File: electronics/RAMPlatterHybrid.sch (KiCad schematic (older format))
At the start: 53 parts, among them J1 Raspberry_Pi_2_3, U1 LM358, U2 74LVC74APW, U3 AV2-8.4-10, U4 AV2-8.4-10, U5 HC4046A, U6 CD74HC4059, U7 AP1117-33, U8 WM8750, U9 NE567

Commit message: v1.0
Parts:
- added J2: Raspberry_Pi_2_3, Connector_PinHeader_2.54mm:PinHeader_2x20_P2.54mm_Vertical, symbol Connector:Raspberry_Pi_2_3
- added JP3: SolderJumper_2_Bridged, Jumper:SolderJumper-2_P1.3mm_Bridged_Pad1.0x1.5mm, symbol Jumper:SolderJumper_2_Bridged
- C10, C16, C8: footprint (none) -> Capacitor_SMD:CP_Elec_4x5.3
- C11, C12, C13, C14: value 1u -> 1u NP; footprint (none) -> Capacitor_SMD:CP_Elec_5x5.3
- C24: footprint Capacitor_SMD:C_0603_1608Metric -> (none)
- C26: renamed from C22; footprint Capacitor_SMD:C_0603_1608Metric -> (none)
- J1: footprint Connector_PinHeader_2.54mm:PinHeader_2x20_P2.54mm_Vertical -> 40pin.SMD.rev:02x20.SMD.pinLocsRev
- R10, R7, R8, R9: value 47R -> 75R
- R13, R14, R15: footprint Resistor_SMD:R_0603_1608Metric -> (none)
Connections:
- net +3V3: now also J2.17 (3V3); no longer J1.1 (3V3)
- net +5V: now also J2.2 (5V), J2.4 (5V)
- net GND: now also J2.14 (GND), J2.20 (GND), J2.25 (GND), J2.30 (GND), J2.34 (GND), J2.39 (GND), J2.6 (GND), J2.9 (GND), JP3.2 (B)
- net GNDA: now also JP3.1 (A)
- net HIGH: now also U6.14 (KA)
- net LOW: no longer U6.14 (KA)
- net SCL: now also J2.5 (SCL/GPIO3)
- net SDA: now also J2.3 (SDA/GPIO2)
- net at J1.10 (GPIO15/RXD): now also J2.10 (GPIO15/RXD)
- net at J1.11 (GPIO17): now also J2.11 (GPIO17)
- net at J1.13 (GPIO27): now also J2.13 (GPIO27)
- net at J1.15 (GPIO22): now also J2.15 (GPIO22)
- net at J1.16 (GPIO23): now also J2.16 (GPIO23)
- net at J1.18 (GPIO24): now also J2.18 (GPIO24)
- net at J1.19 (MOSI0/GPIO10): now also J2.19 (MOSI0/GPIO10)
- net at J1.21 (MISO0/GPIO9): now also J2.21 (MISO0/GPIO9)
- net at J1.22 (GPIO25): now also J2.22 (GPIO25)
- net at J1.23 (SCLK0/GPIO11): now also J2.23 (SCLK0/GPIO11)
- net at J1.24 (~CE0~/GPIO8): now also J2.24 (~CE0~/GPIO8)
- net at J1.26 (~CE1~/GPIO7): now also J2.26 (~CE1~/GPIO7)
- net at J1.27 (ID_SD/GPIO0): now also J2.27 (ID_SD/GPIO0)
- net at J1.28 (ID_SC/GPIO1): now also J2.28 (ID_SC/GPIO1)
- net at J1.29 (GCLK1/GPIO5): now also J2.29 (GCLK1/GPIO5)
- net at J1.31 (GCLK2/GPIO6): now also J2.31 (GCLK2/GPIO6)
- net at J1.32 (PWM0/GPIO12): now also J2.32 (PWM0/GPIO12)
- net at J1.33 (PWM1/GPIO13): now also J2.33 (PWM1/GPIO13)
- net at J1.36 (GPIO16): now also J2.36 (GPIO16)
- net at J1.7 (GCLK0/GPIO4): now also J2.7 (GCLK0/GPIO4)
- net at J1.8 (GPIO14/TXD): now also J2.8 (GPIO14/TXD)
- net AVDD: now reaches C4.1, C5.1, C6.1, C8.1, U7.2 (VO), U8.17 (HPVDD), U8.18 (AVDD)
- new net: J1.1 (3V3), J2.1 (3V3)
- no-connect marks 15 -> 20

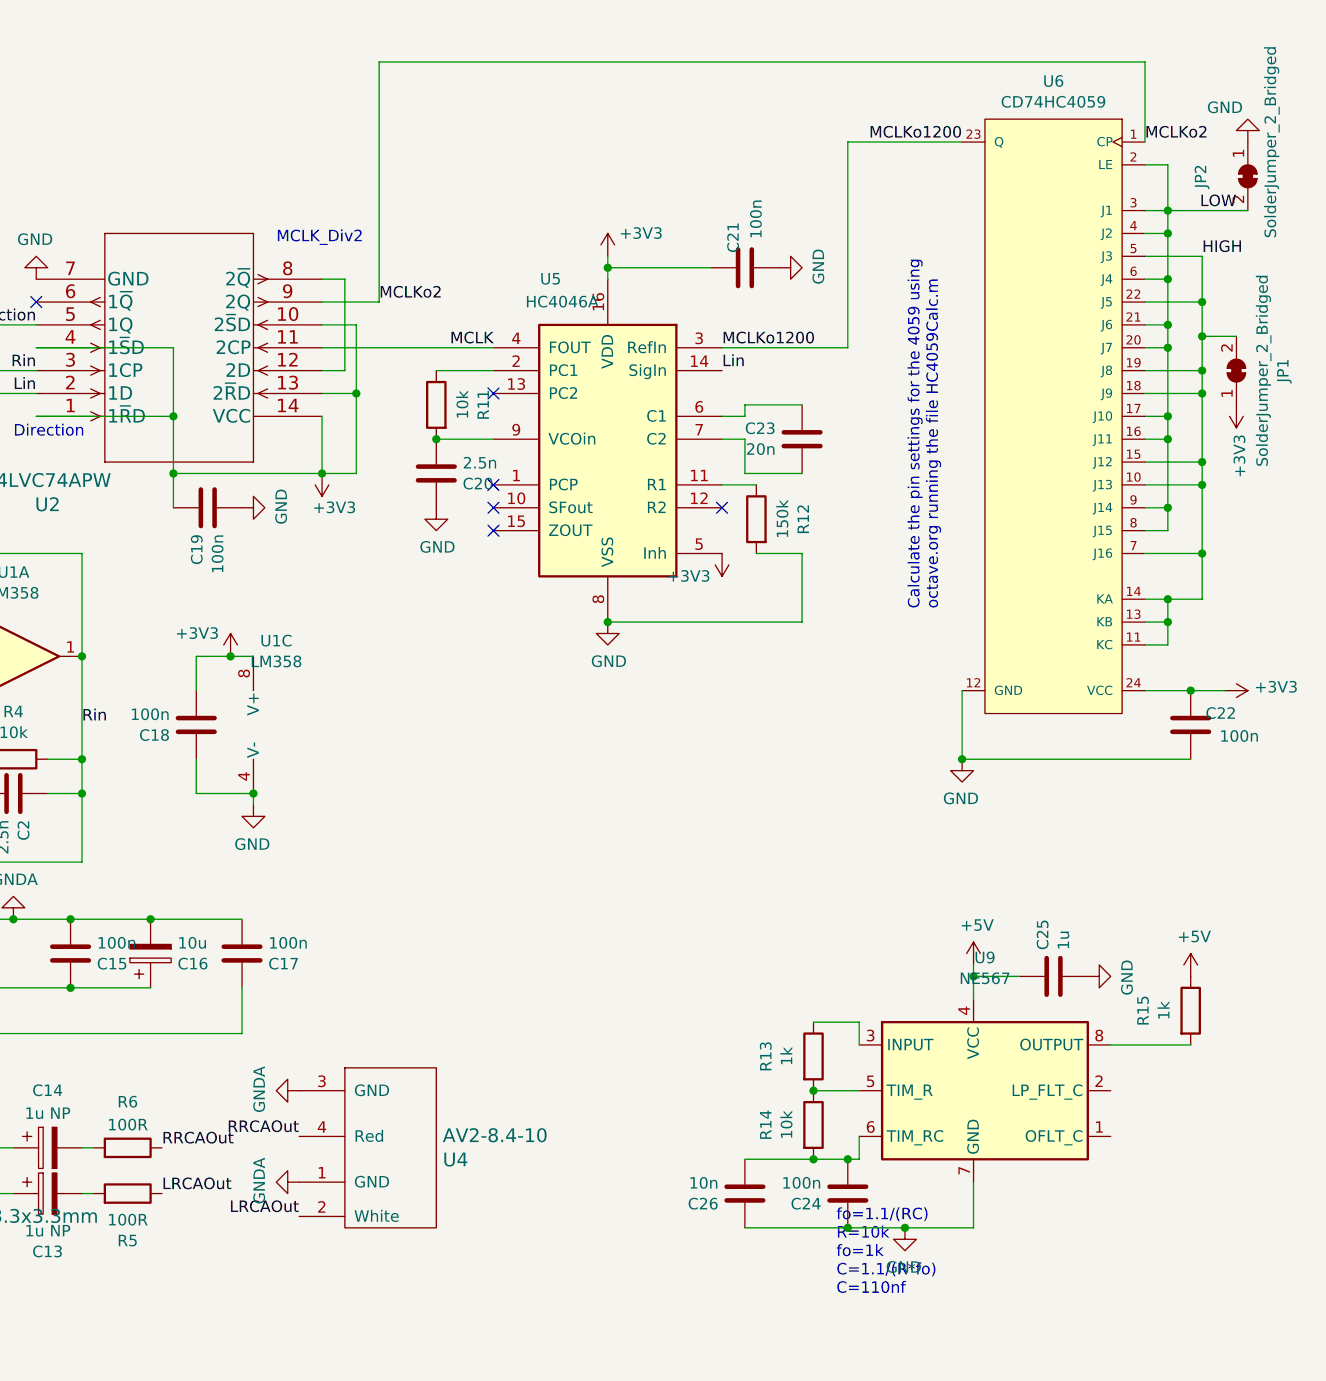
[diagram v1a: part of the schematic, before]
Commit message: v1.1 Many hardware bug fixes, 4059 now dividing correctly. 4046 voc on better target, still debugging 4046 PLL.
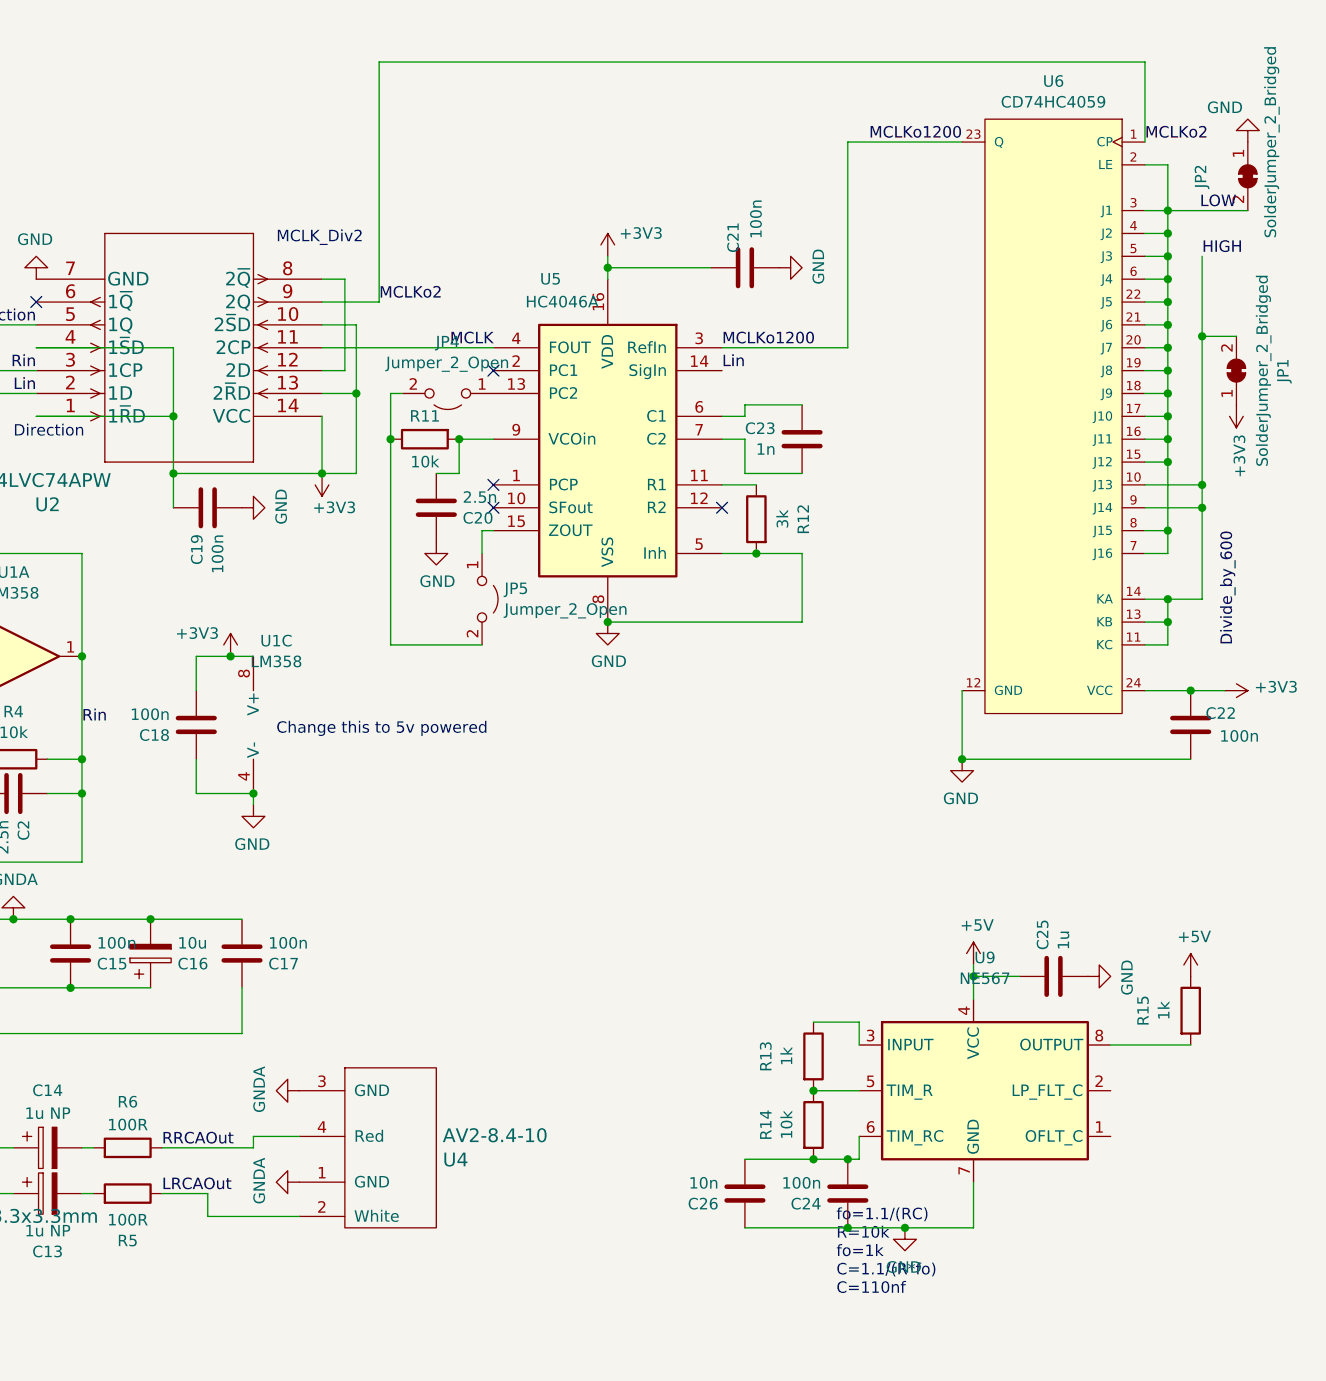
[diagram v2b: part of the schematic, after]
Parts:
- added JP4, JP5: Jumper_2_Open, Jumper:SolderJumper-2_P1.3mm_Open_Pad1.0x1.5mm, symbol Jumper:Jumper_2_Open
- C23: value 20n -> 1n
- R12: value 150k -> 3k
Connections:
- net +3V3: no longer U5.5 (Inh)
- net GND: now also U5.5 (Inh)
- net HIGH: now also U6.9 (J14); no longer U6.15 (J12), U6.18 (J9), U6.19 (J8), U6.22 (J5), U6.5 (J3), U6.7 (J16)
- net LOW: now also U6.15 (J12), U6.18 (J9), U6.19 (J8), U6.22 (J5), U6.5 (J3), U6.7 (J16); no longer U6.9 (J14)
- net at U5.13 (PC2): now also JP4.1 (A)
- net at U5.15 (ZOUT): now also JP5.1 (A)
- net at U5.2 (PC1): no longer R11.1
- new net: JP4.2 (B), JP5.2 (B), R11.1
- no-connect marks 20 -> 19
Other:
- note added: "Change this to 5v powered"
- note removed: "Calculate the pin settings for the 4059 using\noctave.org running the file HC4059Calc.m"
- moved on the sheet: C20, R11
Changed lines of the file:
@@
 Text Label 3450 5050 2    50   ~ 0
 Lin
-Text Label 6850 5800 2    50   ~ 0
-LRCAOut
-Text Label 6850 5450 2    50   ~ 0
-RRCAOut
 $Comp
 L power:GNDA #PWR0117
@@
 	1    0    0    -1
 $EndComp
-$Comp
-L power:+3V3 #PWR0114
-U 1 1 619323EE
-P 8700 2900
-F 0 "#PWR0114" H 8700 2750 50  0001 C CNN
-F 1 "+3V3" H 8750 3000 50  0000 L CNN
-F 2 "" H 8700 2900 50  0001 C CNN
-F 3 "" H 8700 2900 50  0001 C CNN
-	1    8700 2900
-	-1   0    0    1
-$EndComp
 Wire Wire Line
 	9050 2900 9050 3200
@@
 	8850 2600 8700 2600
 NoConn ~ 7700 2600
-NoConn ~ 7700 2200
-Wire Wire Line
-	7450 2400 7700 2400
-Wire Wire Line
-	7700 2100 7450 2100
 Text Label 8700 2000 0    50   ~ 0
 MCLKo1200
@@
 P 8850 2750
 F 0 "R12" V 8643 2750 50  0000 C CNN
-F 1 "150k" V 8734 2750 50  0000 C CNN
+F 1 "3k" V 8734 2750 50  0000 C CNN
 F 2 "Resistor_SMD:R_0603_1608Metric" V 8780 2750 50  0001 C CNN
 F 3 "~" H 8850 2750 50  0001 C CNN
@@
 P 9050 2400
 F 0 "C23" H 9165 2446 50  0000 L CNN
-F 1 "20n" H 9165 2355 50  0000 L CNN
+F 1 "1n" H 9165 2355 50  0000 L CNN
 F 2 "Capacitor_SMD:C_0603_1608Metric" H 9088 2250 50  0001 C CNN
 F 3 "~" H 9050 2400 50  0001 C CNN
@@
 L Device:C C20
 U 1 1 61B4B373
-P 7450 2550
-F 0 "C20" H 7565 2596 50  0000 L CNN
-F 1 "2.5n" H 7565 2505 50  0000 L CNN
-F 2 "Capacitor_SMD:C_0603_1608Metric" H 7488 2400 50  0001 C CNN
-F 3 "~" H 7450 2550 50  0001 C CNN
-	1    7450 2550
-	1    0    0    1
-$EndComp
-Connection ~ 7450 2400
+P 7450 2700
+F 0 "C20" H 7565 2746 50  0000 L CNN
+F 1 "2.5n" H 7565 2655 50  0000 L CNN
+F 2 "Capacitor_SMD:C_0603_1608Metric" H 7488 2550 50  0001 C CNN
+F 3 "~" H 7450 2700 50  0001 C CNN
+	1    7450 2700
+	1    0    0    1
+$EndComp
 $Comp
 L Device:R R11
 U 1 1 61B4AD34
-P 7450 2250
-F 0 "R11" V 7243 2250 50  0000 C CNN
-F 1 "10k" V 7334 2250 50  0000 C CNN
-F 2 "Resistor_SMD:R_0603_1608Metric" V 7380 2250 50  0001 C CNN
-F 3 "~" H 7450 2250 50  0001 C CNN
-	1    7450 2250
-	-1   0    0    -1
+P 7400 2400
+F 0 "R11" V 7300 2400 50  0000 C CNN
+F 1 "10k" V 7500 2400 50  0000 C CNN
+F 2 "Resistor_SMD:R_0603_1608Metric" V 7330 2400 50  0001 C CNN
+F 3 "~" H 7400 2400 50  0001 C CNN
+	1    7400 2400
+	0    -1   1    0
 $EndComp
 $Comp
@@
 	-1   0    0    -1
 $EndComp
-NoConn ~ 7700 2800
 NoConn ~ 7700 2700
 $Comp
 L power:GND #PWR0113
 U 1 1 61900830
-P 7450 2700
-F 0 "#PWR0113" H 7450 2450 50  0001 C CNN
-F 1 "GND" H 7455 2527 50  0000 C CNN
-F 2 "" H 7450 2700 50  0001 C CNN
-F 3 "" H 7450 2700 50  0001 C CNN
-	1    7450 2700
+P 7450 2850
+F 0 "#PWR0113" H 7450 2600 50  0001 C CNN
+F 1 "GND" H 7455 2677 50  0000 C CNN
+F 2 "" H 7450 2850 50  0001 C CNN
+F 3 "" H 7450 2850 50  0001 C CNN
+	1    7450 2850
 	1    0    0    -1
 $EndComp
@@
 Wire Wire Line
 	10650 2800 10550 2800
-Wire Wire Line
-	10650 2700 10650 2800
-Connection ~ 10650 2700
-Wire Wire Line
-	10650 2700 10550 2700
 $Comp
 L Jumper:SolderJumper_2_Bridged JP1
@@
 Text Label 10800 1600 0    50   ~ 0
 HIGH
-Text Notes 9650 3150 1    50   ~ 0
-Calculate the pin settings for the 4059 using\noctave.org running the file HC4059Calc.m
 $Comp
 L power:+3V3 #PWR05
@@
 	1    0    0    1
 $EndComp
-Wire Wire Line
-	10800 1600 10550 1600
-Wire Wire Line
-	10800 1800 10800 1950
-Wire Wire Line
-	10800 1800 10800 1600
-Connection ~ 10800 1800
-Wire Wire Line
-	10800 1800 10550 1800
-Wire Wire Line
-	10800 1950 10800 2100
-Connection ~ 10800 2100
-Wire Wire Line
-	10800 2100 10550 2100
-Wire Wire Line
-	10800 2200 10800 2100
-Connection ~ 10800 2200
-Wire Wire Line
-	10800 2200 10550 2200
-Wire Wire Line
-	10800 2500 10800 2200
-Connection ~ 10800 2500
-Wire Wire Line
-	10800 2500 10550 2500
-Wire Wire Line
-	10800 2600 10800 2500
 Connection ~ 10800 2600
 Wire Wire Line
@@
 	1    0    0    1
 $EndComp
-Wire Wire Line
-	10650 2400 10650 2700
 Connection ~ 10650 2400
 Wire Wire Line
@@
 	10650 2300 10550 2300
 Wire Wire Line
-	10650 2000 10650 2300
+	10650 2000 10650 2100
 Connection ~ 10650 2000
 Wire Wire Line
@@
 	10650 1900 10550 1900
 Wire Wire Line
-	10650 1700 10650 1900
+	10650 1700 10650 1800
 Connection ~ 10650 1700
 Wire Wire Line
 	10650 1700 10550 1700
 Wire Wire Line
-	10650 1500 10650 1700
+	10650 1500 10650 1600
 Wire Wire Line
 	10650 1400 10650 1500
@@
 Wire Wire Line
 	10650 3100 10550 3100
-Wire Wire Line
-	10800 2900 10800 2600
-Wire Wire Line
-	10550 2900 10800 2900
 $Comp
 L Device:C C22
@@
 Wire Wire Line
 	10650 3100 10800 3100
-Wire Wire Line
-	10800 3100 10800 2900
 Connection ~ 10650 3100
-Connection ~ 10800 2900
 Wire Wire Line
 	10550 3200 10650 3200
@@
 Wire Wire Line
 	1950 6200 1950 6000
+Text Notes 6750 3700 0    50   ~ 0
+Change this to 5v powered
+Wire Wire Line
+	10800 1600 10800 1950
+Wire Wire Line
+	10800 1950 10800 2600
+Wire Wire Line
+	10650 2400 10650 2500
+Wire Wire Line
+	10550 1600 10650 1600
+Connection ~ 10650 1600
+Wire Wire Line
+	10650 1600 10650 1700
+Wire Wire Line
+	10550 1800 10650 1800
+Connection ~ 10650 1800
+Wire Wire Line
+	10650 1800 10650 1900
+Wire Wire Line
+	10550 2100 10650 2100
+Connection ~ 10650 2100
+Wire Wire Line
+	10650 2100 10650 2200
+Wire Wire Line
+	10550 2200 10650 2200
+Connection ~ 10650 2200
+Wire Wire Line
+	10650 2200 10650 2300
+Wire Wire Line
+	10550 2500 10650 2500
+Connection ~ 10650 2500
+Wire Wire Line
+	10650 2500 10650 2800
+Wire Wire Line
+	10550 2700 10800 2700
+Connection ~ 10800 2700
+Wire Wire Line
+	10800 2700 10800 2600
+Wire Wire Line
+	10800 2700 10800 3100
+Wire Wire Line
+	10650 2800 10650 2900
+Wire Wire Line
+	10650 2900 10550 2900
+Connection ~ 10650 2800
+NoConn ~ 7700 2100
+Text Label 10950 3300 1    50   ~ 0
+Divide_by_600
+Wire Wire Line
+	8700 2900 8850 2900
+Connection ~ 8850 2900
+$Comp
+L Jumper:Jumper_2_Open JP5
+U 1 1 61B5D1B6
+P 7650 3100
+F 0 "JP5" V 7604 3198 50  0000 L CNN
+F 1 "Jumper_2_Open" V 7695 3198 50  0000 L CNN
+F 2 "Jumper:SolderJumper-2_P1.3mm_Open_Pad1.0x1.5mm" H 7650 3100 50  0001 C CNN
+F 3 "~" H 7650 3100 50  0001 C CNN
+	1    7650 3100
+	0    1    1    0
+$EndComp
+Wire Wire Line
+	7700 2800 7650 2800
+Wire Wire Line
+	7650 2800 7650 2900
+Wire Wire Line
+	7450 2550 7550 2550
+Wire Wire Line
+	7550 2550 7550 2400
+Wire Wire Line
+	7550 2400 7700 2400
+Connection ~ 7550 2400
+$Comp
+L Jumper:Jumper_2_Open JP4
+U 1 1 61BE7076
+P 7500 2200
+F 0 "JP4" H 7500 1975 50  0000 C CNN
+F 1 "Jumper_2_Open" H 7500 2066 50  0000 C CNN
+F 2 "Jumper:SolderJumper-2_P1.3mm_Open_Pad1.0x1.5mm" H 7500 2200 50  0001 C CNN
+F 3 "~" H 7500 2200 50  0001 C CNN
+	1    7500 2200
+	-1   0    0    1
+$EndComp
+Wire Wire Line
+	7300 2200 7250 2200
+Wire Wire Line
+	7250 2200 7250 2400
+Wire Wire Line
+	7650 3300 7250 3300
+Wire Wire Line
+	7250 3300 7250 2400
+Connection ~ 7250 2400
+Wire Wire Line
+	6250 5500 6650 5500
+Wire Wire Line
+	6650 5500 6650 5450
+Wire Wire Line
+	6650 5450 6850 5450
+Wire Wire Line
+	6250 5700 6450 5700
+Wire Wire Line
+	6450 5700 6450 5800
+Wire Wire Line
+	6450 5800 6850 5800
 $EndSCHEMATC

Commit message: added a pdf
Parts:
- removed C24: 100n, symbol Device:C
- removed C25: 1u, symbol Device:C
- removed C26: 10n, symbol Device:C
- removed R13, R15: 1k, symbol Device:R
- removed R14: 10k, symbol Device:R
- removed U9: NE567, symbol Timer:NE567
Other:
- note removed: "fo=1.1/(RC)\nR=10k\nfo=1k\nC=1.1/(R*fo)\nC=110nf"
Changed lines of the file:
@@
 	10650 3200 10650 3300
-$Comp
-L Timer:NE567 U9
-U 1 1 619FBBE5
-P 9800 5250
-F 0 "U9" H 9850 5831 50  0000 C CNN
-F 1 "NE567" H 9850 5740 50  0000 C CNN
-F 2 "" H 9850 4900 50  0001 L CNN
-F 3 "http://www.ti.com/lit/ds/symlink/lm567.pdf" H 9500 5250 50  0001 C CNN
-	1    9800 5250
-	1    0    0    -1
-$EndComp
-Wire Wire Line
-	9250 5550 9100 5550
-$Comp
-L Device:C C24
-U 1 1 61A0E20C
-P 9250 5700
-F 0 "C24" H 9365 5746 50  0000 L CNN
-F 1 "100n" H 9365 5655 50  0000 L CNN
-F 2 "" H 9288 5550 50  0001 C CNN
-F 3 "~" H 9250 5700 50  0001 C CNN
-	1    9250 5700
-	-1   0    0    1
-$EndComp
-Connection ~ 9250 5850
-Wire Wire Line
-	8800 5850 9250 5850
-Connection ~ 9250 5550
-Wire Wire Line
-	9300 5550 9250 5550
-$Comp
-L Device:C C25
-U 1 1 61A193DE
-P 10150 4750
-F 0 "C25" H 10265 4796 50  0000 L CNN
-F 1 "1u" H 10265 4705 50  0000 L CNN
-F 2 "" H 10188 4600 50  0001 C CNN
-F 3 "~" H 10150 4750 50  0001 C CNN
-	1    10150 4750
-	0    -1   -1   0
-$EndComp
-$Comp
-L Device:R R15
-U 1 1 61A33E22
-P 10750 4900
-F 0 "R15" V 10543 4900 50  0000 C CNN
-F 1 "1k" V 10634 4900 50  0000 C CNN
-F 2 "" V 10680 4900 50  0001 C CNN
-F 3 "~" H 10750 4900 50  0001 C CNN
-	1    10750 4900
-	1    0    0    -1
-$EndComp
-Wire Wire Line
-	9100 5250 9300 5250
-Wire Wire Line
-	9300 5450 9300 5550
-Wire Wire Line
-	9800 5650 9800 5850
-Wire Wire Line
-	9500 5850 9250 5850
-Wire Wire Line
-	9800 5850 9500 5850
-Connection ~ 9500 5850
-$Comp
-L power:GND #PWR0102
-U 1 1 61A16162
-P 9500 5850
-F 0 "#PWR0102" H 9500 5600 50  0001 C CNN
-F 1 "GND" H 9505 5677 50  0000 C CNN
-F 2 "" H 9500 5850 50  0001 C CNN
-F 3 "" H 9500 5850 50  0001 C CNN
-	1    9500 5850
-	-1   0    0    -1
-$EndComp
-$Comp
-L power:+5V #PWR0103
-U 1 1 61A18806
-P 9800 4700
-F 0 "#PWR0103" H 9800 4550 50  0001 C CNN
-F 1 "+5V" H 9815 4873 50  0000 C CNN
-F 2 "" H 9800 4700 50  0001 C CNN
-F 3 "" H 9800 4700 50  0001 C CNN
-	1    9800 4700
-	1    0    0    -1
-$EndComp
-Wire Wire Line
-	10000 4750 9800 4750
-Wire Wire Line
-	9800 4750 9800 4700
-Connection ~ 9800 4750
-Wire Wire Line
-	9800 4850 9800 4750
-$Comp
-L power:GND #PWR0104
-U 1 1 61A295BD
-P 10300 4750
-F 0 "#PWR0104" H 10300 4500 50  0001 C CNN
-F 1 "GND" H 10305 4577 50  0000 C CNN
-F 2 "" H 10300 4750 50  0001 C CNN
-F 3 "" H 10300 4750 50  0001 C CNN
-	1    10300 4750
-	0    -1   1    0
-$EndComp
-Wire Wire Line
-	9300 5050 9300 4950
-Wire Wire Line
-	9300 4950 9100 4950
-Wire Wire Line
-	10750 5050 10400 5050
-$Comp
-L power:+5V #PWR0105
-U 1 1 61A3CC92
-P 10750 4750
-F 0 "#PWR0105" H 10750 4600 50  0001 C CNN
-F 1 "+5V" H 10765 4923 50  0000 C CNN
-F 2 "" H 10750 4750 50  0001 C CNN
-F 3 "" H 10750 4750 50  0001 C CNN
-	1    10750 4750
-	1    0    0    -1
-$EndComp
-Text Notes 9200 6150 0    50   ~ 0
-fo=1.1/(RC)\nR=10k\nfo=1k\nC=1.1/(R*fo)\nC=110nf
-$Comp
-L Device:R R14
-U 1 1 619FFDBB
-P 9100 5400
-F 0 "R14" V 8893 5400 50  0000 C CNN
-F 1 "10k" V 8984 5400 50  0000 C CNN
-F 2 "" V 9030 5400 50  0001 C CNN
-F 3 "~" H 9100 5400 50  0001 C CNN
-	1    9100 5400
-	1    0    0    -1
-$EndComp
-Connection ~ 9100 5550
-Wire Wire Line
-	8800 5550 9100 5550
-Connection ~ 9100 5250
-$Comp
-L Device:R R13
-U 1 1 61A2A6B6
-P 9100 5100
-F 0 "R13" V 8893 5100 50  0000 C CNN
-F 1 "1k" V 8984 5100 50  0000 C CNN
-F 2 "" V 9030 5100 50  0001 C CNN
-F 3 "~" H 9100 5100 50  0001 C CNN
-	1    9100 5100
-	1    0    0    -1
-$EndComp
-$Comp
-L Device:C C26
-U 1 1 61A3FC52
-P 8800 5700
-F 0 "C26" H 8915 5746 50  0000 L CNN
-F 1 "10n" H 8915 5655 50  0000 L CNN
-F 2 "" H 8838 5550 50  0001 C CNN
-F 3 "~" H 8800 5700 50  0001 C CNN
-	1    8800 5700
-	-1   0    0    1
-$EndComp
 $Comp
 L Connector:Raspberry_Pi_2_3 J2
